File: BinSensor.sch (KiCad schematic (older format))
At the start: 16 parts

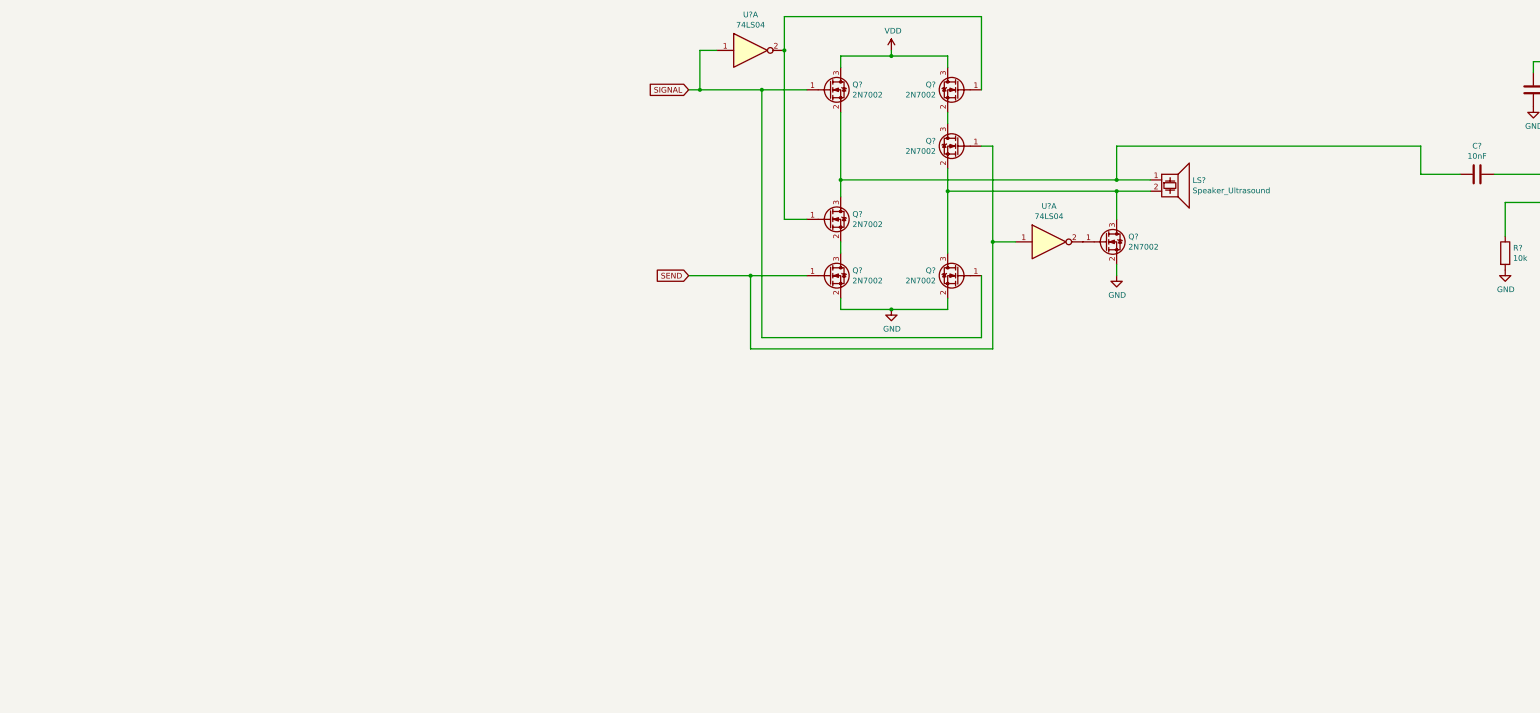
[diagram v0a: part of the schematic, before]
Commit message: Rough outline of transformer and h-bridge based drivers. Need to determine protection device for AFE.
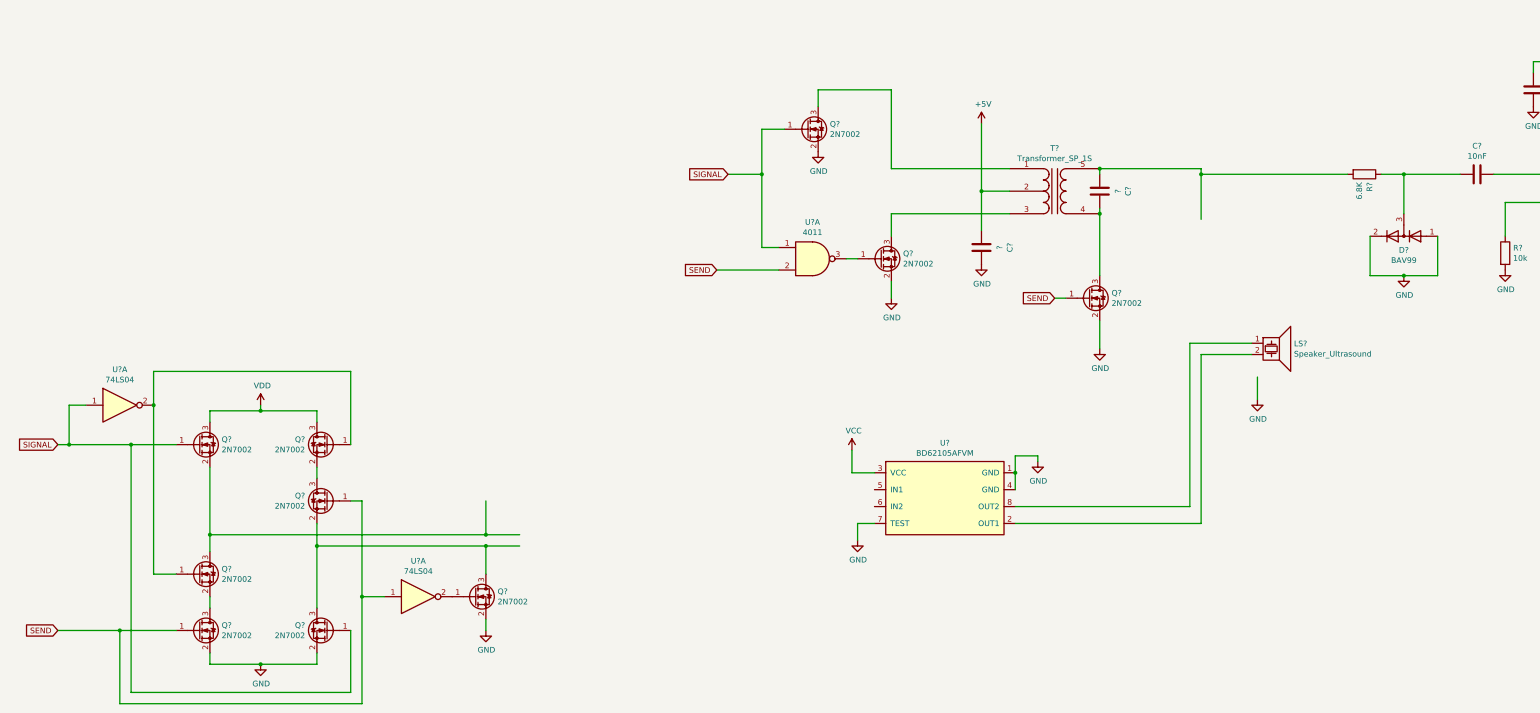
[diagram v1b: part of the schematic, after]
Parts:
- added C? (x2): ?, symbol Device:C
- added D?: BAV99, Package_TO_SOT_SMD:SOT-23, symbol Diode:BAV99
- added Q? (x3): 2N7002, Package_TO_SOT_SMD:SOT-23, symbol Transistor_FET:2N7002
- added R?: 6.8K, symbol Device:R
- added T?: Transformer_SP_1S, symbol Device:Transformer_SP_1S
- added U?: 4011, symbol 4xxx:4011
- added U?: BD62105AFVM, symbol Bin_Sensor:BD62105AFVM
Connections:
- net labels added: +5V, VCC
- wire segments 68 -> 113
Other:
- moved on the sheet: LS?, Q?, U?A

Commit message: Changed input SIGNAL and RxTx drive signal to use a NOR verus NAND. Found NOR gate IC.
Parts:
- removed U?: 4011, symbol 4xxx:4011
- added Q?: 2N7002, Package_TO_SOT_SMD:SOT-23, symbol Transistor_FET:2N7002
- added R?: 0, symbol Device:R
- added U? (x2): 74LVC1G02, symbol 74xGxx:74LVC1G02
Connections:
- net labels added: RxTx
- wire segments 113 -> 129
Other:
- moved on the sheet: Q?
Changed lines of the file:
@@
 Wire Wire Line
 	4500 2000 4500 2050
-Wire Wire Line
-	4500 2350 4500 2400
-Wire Wire Line
-	4500 2400 4500 2950
-Connection ~ 4500 2400
 $Comp
 L power:GND #PWR?
 U 1 1 617E9294
-P 4500 3600
-F 0 "#PWR?" H 4500 3350 50  0001 C CNN
-F 1 "GND" H 4505 3427 50  0000 C CNN
-F 2 "" H 4500 3600 50  0001 C CNN
-F 3 "" H 4500 3600 50  0001 C CNN
-	1    4500 3600
-	1    0    0    -1
-$EndComp
-Wire Wire Line
-	4500 3350 4500 3600
-Text GLabel 4100 3150 0    50   Input ~ 0
-SEND
-Wire Wire Line
-	4200 3150 4100 3150
+P 5800 4550
+F 0 "#PWR?" H 5800 4300 50  0001 C CNN
+F 1 "GND" H 5805 4377 50  0000 C CNN
+F 2 "" H 5800 4550 50  0001 C CNN
+F 3 "" H 5800 4550 50  0001 C CNN
+	1    5800 4550
+	1    0    0    -1
+$EndComp
+Text GLabel 5400 4250 0    50   Input ~ 0
+RxTx
+Wire Wire Line
+	5500 4250 5400 4250
 $Comp
 L Transistor_FET:2N7002 Q?
 U 1 1 6182813E
-P 4400 3150
-F 0 "Q?" H 4605 3196 50  0000 L CNN
-F 1 "2N7002" H 4605 3105 50  0000 L CNN
-F 2 "Package_TO_SOT_SMD:SOT-23" H 4600 3075 50  0001 L CIN
-F 3 "https://www.onsemi.com/pub/Collateral/NDS7002A-D.PDF" H 4400 3150 50  0001 L CNN
-	1    4400 3150
+P 5700 4250
+F 0 "Q?" H 5905 4296 50  0000 L CNN
+F 1 "2N7002" H 5905 4205 50  0000 L CNN
+F 2 "Package_TO_SOT_SMD:SOT-23" H 5900 4175 50  0001 L CIN
+F 3 "https://www.onsemi.com/pub/Collateral/NDS7002A-D.PDF" H 5700 4250 50  0001 L CNN
+	1    5700 4250
 	1    0    0    -1
 $EndComp
@@
 	1    0    0    -1
 $EndComp
-Text GLabel 1100 2900 0    50   Input ~ 0
-SEND
-$Comp
-L 4xxx:4011 U?
-U 1 1 6199AE61
-P 1950 2800
-F 0 "U?" H 1950 3125 50  0000 C CNN
-F 1 "4011" H 1950 3034 50  0000 C CNN
-F 2 "" H 1950 2800 50  0001 C CNN
-F 3 "http://www.intersil.com/content/dam/Intersil/documents/cd40/cd4011bms-12bms-23bms.pdf" H 1950 2800 50  0001 C CNN
-	1    1950 2800
-	1    0    0    -1
-$EndComp
-Wire Wire Line
-	1500 2050 1500 2700
-Wire Wire Line
-	1500 2700 1650 2700
-Connection ~ 1500 2050
-Wire Wire Line
-	1100 2900 1650 2900
 $Comp
 L Diode:BAV99 D?
@@
 	-1   0    0    1
 $EndComp
-$Comp
-L power:GND #PWR?
-U 1 1 617D8C54
-P 5900 4050
-F 0 "#PWR?" H 5900 3800 50  0001 C CNN
-F 1 "GND" H 5905 3877 50  0000 C CNN
-F 2 "" H 5900 4050 50  0001 C CNN
-F 3 "" H 5900 4050 50  0001 C CNN
-	1    5900 4050
-	1    0    0    -1
-$EndComp
-Wire Wire Line
-	5900 4050 5900 3850
 Wire Wire Line
 	7500 2600 7500 2950
@@
 Wire Wire Line
 	7200 2050 7700 2050
-Wire Wire Line
-	5400 2450 5400 2050
-Wire Wire Line
-	5400 2050 6700 2050
-Wire Wire Line
-	5400 2050 5400 2000
-Wire Wire Line
-	5400 2000 4500 2000
-Connection ~ 5400 2050
-Connection ~ 4500 2000
 $Comp
 L Bin_Sensor:BD62105AFVM U?
 U 1 1 619E0BA6
 P 3100 4900
-F 0 "U?" H 3125 5365 50  0000 C CNN
-F 1 "BD62105AFVM" H 3125 5274 50  0000 C CNN
+F 0 "U?" H 3100 5000 50  0000 C CNN
+F 1 "BD62105AFVM" H 3100 4900 50  0000 C CNN
 F 2 "" H 3100 4900 50  0001 C CNN
 F 3 "" H 3100 4900 50  0001 C CNN
@@
 	3950 4550 3950 4600
 Connection ~ 3750 4700
-Wire Wire Line
-	3750 5000 5300 5000
-Wire Wire Line
-	5300 5000 5300 3550
-Wire Wire Line
-	5300 3550 5850 3550
-Wire Wire Line
-	5850 3650 5400 3650
-Wire Wire Line
-	5400 3650 5400 5150
-Wire Wire Line
-	5400 5150 3750 5150
+Connection ~ 1500 2050
+Wire Wire Line
+	1150 2850 1700 2850
+Text GLabel 1150 2850 0    50   Input ~ 0
+RxTx
+Text GLabel 1100 4450 0    50   Input ~ 0
+SIGNAL
+Wire Wire Line
+	1100 4450 1250 4450
+Wire Wire Line
+	1250 4450 2150 4450
+Wire Wire Line
+	2150 4450 2150 4850
+Wire Wire Line
+	2150 4850 2500 4850
+Connection ~ 1250 4450
+Text GLabel 1100 5050 0    50   Input ~ 0
+RxTx
+Wire Wire Line
+	1100 5050 1400 5050
+Wire Wire Line
+	1950 5000 2500 5000
+Wire Wire Line
+	5800 4450 5800 4550
+Wire Wire Line
+	5800 4050 5800 3900
+Wire Wire Line
+	5800 3550 5800 2050
+Wire Wire Line
+	5800 2050 6700 2050
+Connection ~ 5800 3550
+Wire Wire Line
+	5800 3550 5850 3550
+Wire Wire Line
+	4250 3650 4250 5150
+Wire Wire Line
+	4250 5150 3750 5150
+Wire Wire Line
+	4150 3550 4150 5000
+Wire Wire Line
+	4150 5000 3750 5000
+Wire Wire Line
+	4150 3550 5800 3550
+Wire Wire Line
+	4500 2000 5800 2000
+Wire Wire Line
+	5800 2000 5800 2050
+Connection ~ 4500 2000
+Connection ~ 5800 2050
+Wire Wire Line
+	4500 2350 4500 2400
+Connection ~ 4500 2400
+Connection ~ 5800 3650
+Wire Wire Line
+	5800 3650 5850 3650
+Wire Wire Line
+	4250 3650 5800 3650
+$Comp
+L power:GND #PWR?
+U 1 1 61B18D45
+P 4500 3100
+F 0 "#PWR?" H 4500 2850 50  0001 C CNN
+F 1 "GND" H 4505 2927 50  0000 C CNN
+F 2 "" H 4500 3100 50  0001 C CNN
+F 3 "" H 4500 3100 50  0001 C CNN
+	1    4500 3100
+	1    0    0    -1
+$EndComp
+Text GLabel 4100 2800 0    50   Input ~ 0
+RxTx
+Wire Wire Line
+	4200 2800 4100 2800
+$Comp
+L Transistor_FET:2N7002 Q?
+U 1 1 61B18D4D
+P 4400 2800
+F 0 "Q?" H 4605 2846 50  0000 L CNN
+F 1 "2N7002" H 4605 2755 50  0000 L CNN
+F 2 "Package_TO_SOT_SMD:SOT-23" H 4600 2725 50  0001 L CIN
+F 3 "https://www.onsemi.com/pub/Collateral/NDS7002A-D.PDF" H 4400 2800 50  0001 L CNN
+	1    4400 2800
+	1    0    0    -1
+$EndComp
+Wire Wire Line
+	4500 3000 4500 3100
+Wire Wire Line
+	4500 2400 4500 2600
+$Comp
+L Device:R R?
+U 1 1 61B32646
+P 6450 4250
+F 0 "R?" H 6520 4296 50  0000 L CNN
+F 1 "0" H 6520 4205 50  0000 L CNN
+F 2 "" V 6380 4250 50  0001 C CNN
+F 3 "~" H 6450 4250 50  0001 C CNN
+	1    6450 4250
+	1    0    0    -1
+$EndComp
+Wire Wire Line
+	5800 3900 6450 3900
+Wire Wire Line
+	6450 3900 6450 4100
+Connection ~ 5800 3900
+Wire Wire Line
+	5800 3900 5800 3650
+$Comp
+L power:GND #PWR?
+U 1 1 61B389B6
+P 6450 4550
+F 0 "#PWR?" H 6450 4300 50  0001 C CNN
+F 1 "GND" H 6455 4377 50  0000 C CNN
+F 2 "" H 6450 4550 50  0001 C CNN
+F 3 "" H 6450 4550 50  0001 C CNN
+	1    6450 4550
+	1    0    0    -1
+$EndComp
+Wire Wire Line
+	6450 4550 6450 4400
+Wire Wire Line
+	1700 2750 1500 2750
+Wire Wire Line
+	1500 2050 1500 2750
+Wire Wire Line
+	1400 4950 1250 4950
+Wire Wire Line
+	1250 4450 1250 4950
+$Comp
+L 74xGxx:74LVC1G02 U?
+U 1 1 61B97BFE
+P 2000 2800
+F 0 "U?" H 1975 3067 50  0000 C CNN
+F 1 "74LVC1G02" H 1975 2976 50  0000 C CNN
+F 2 "" H 2000 2800 50  0001 C CNN
+F 3 "http://www.ti.com/lit/sg/scyt129e/scyt129e.pdf" H 2000 2800 50  0001 C CNN
+	1    2000 2800
+	1    0    0    -1
+$EndComp
+$Comp
+L 74xGxx:74LVC1G02 U?
+U 1 1 61B9F815
+P 1700 5000
+F 0 "U?" H 1675 5267 50  0000 C CNN
+F 1 "74LVC1G02" H 1675 5176 50  0000 C CNN
+F 2 "" H 1700 5000 50  0001 C CNN
+F 3 "http://www.ti.com/lit/sg/scyt129e/scyt129e.pdf" H 1700 5000 50  0001 C CNN
+	1    1700 5000
+	1    0    0    -1
+$EndComp
 $EndSCHEMATC

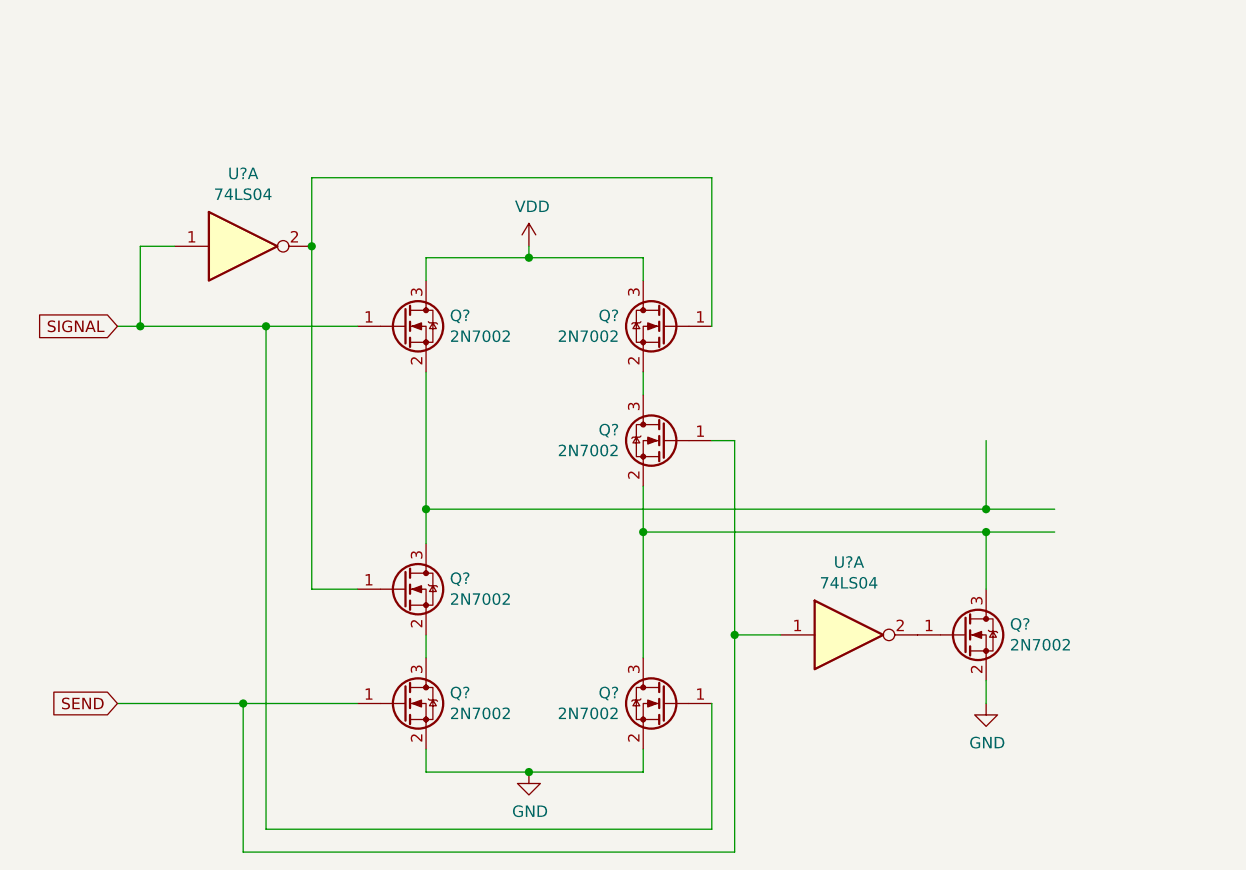
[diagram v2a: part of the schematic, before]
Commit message: Deleted old H-bridge circuit.
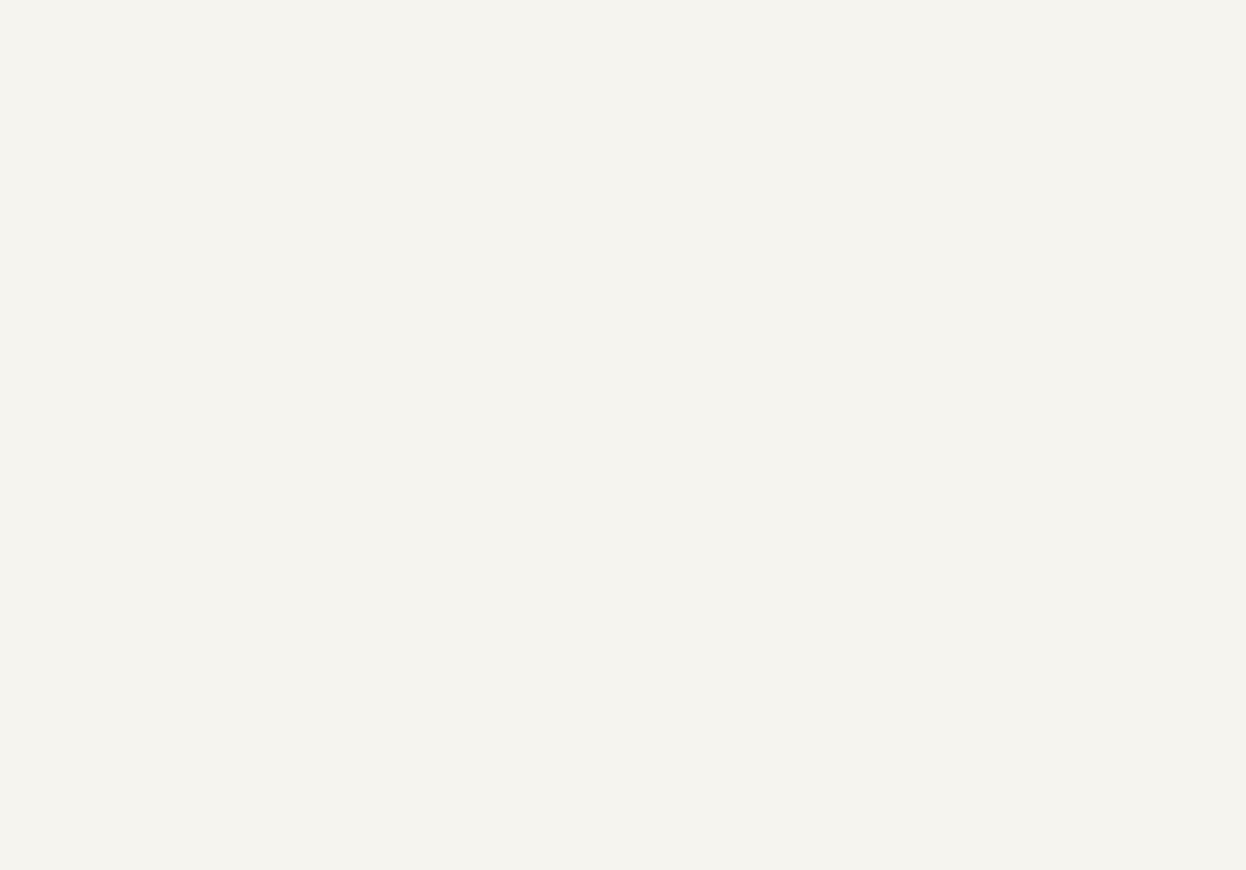
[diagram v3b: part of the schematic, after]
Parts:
- removed Q? (x7): 2N7002, Package_TO_SOT_SMD:SOT-23, symbol Transistor_FET:2N7002
- removed U? (x2): 74LS04, symbol 74xx:74LS04
